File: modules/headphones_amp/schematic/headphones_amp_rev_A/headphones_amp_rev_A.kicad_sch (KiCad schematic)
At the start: 41 parts, among them J1 AudioJack3_SwitchTR, Q1 BC140, Q2 BC160, Q3 BC548, Q4 BC557, Q5 BC548, Q6 BC548, Q7 BC548, Q8 BC557

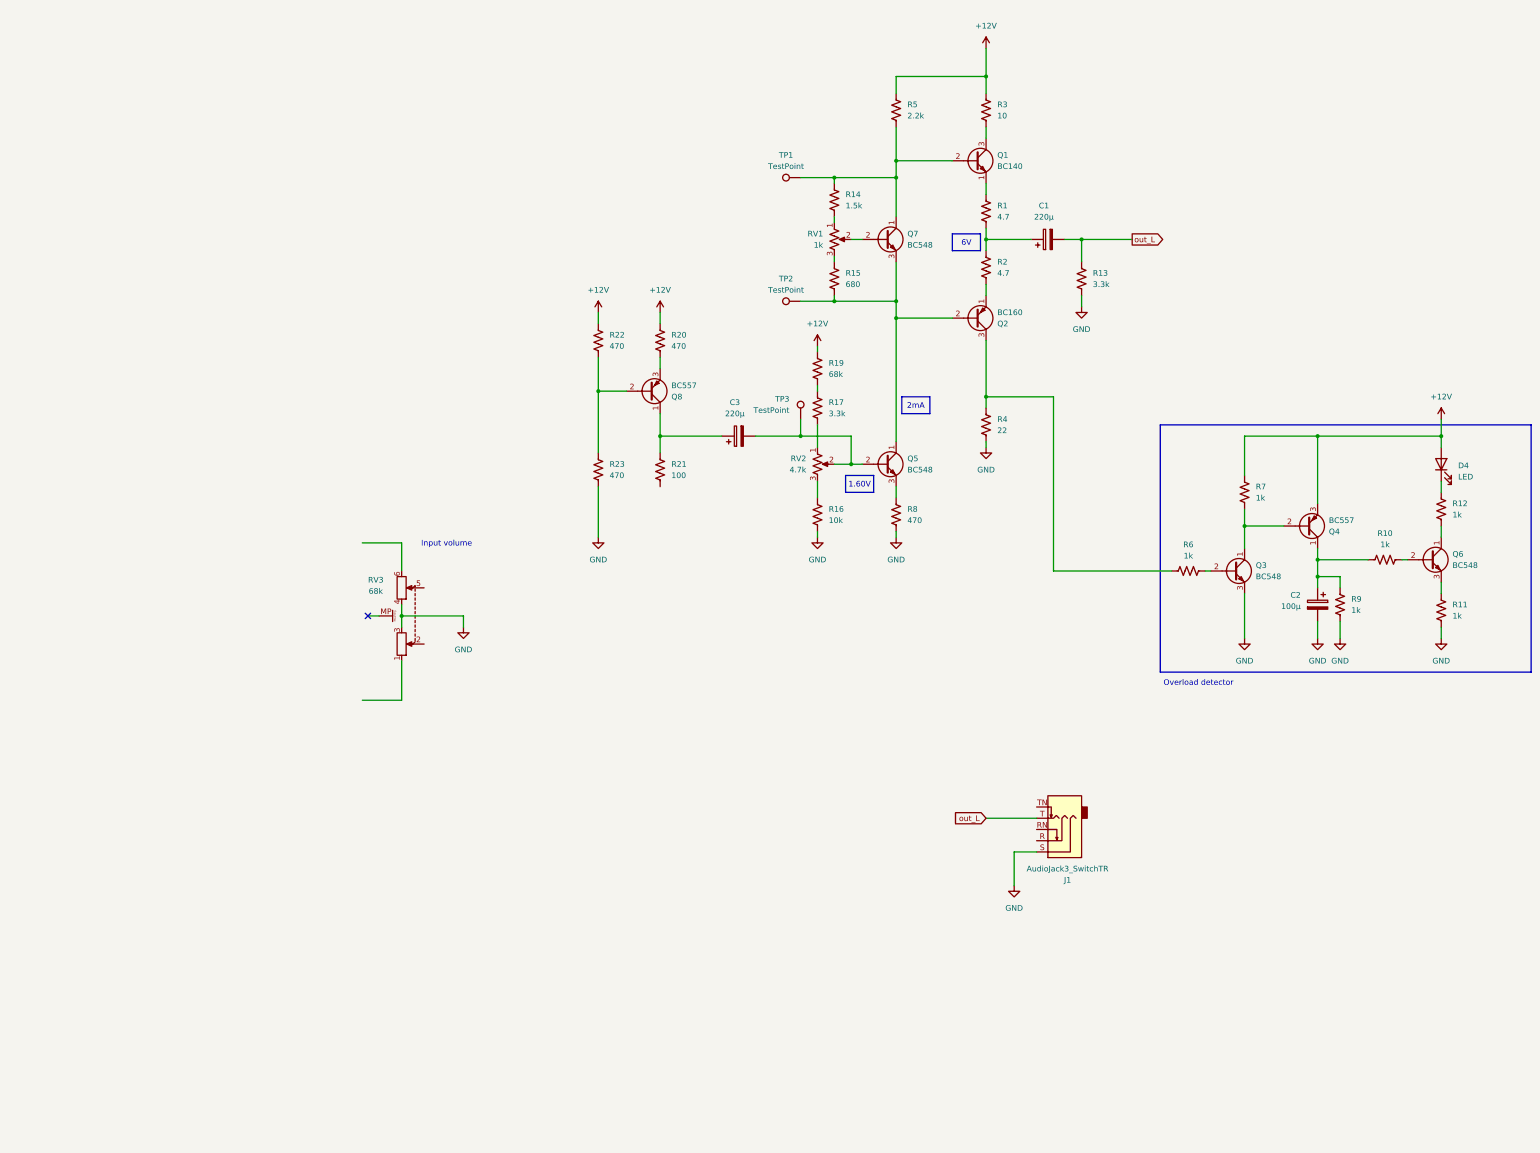
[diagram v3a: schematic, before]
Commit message: updated the Bourns PTV112 updated schematic renamed and upgraded the list of commonly used kicad parts
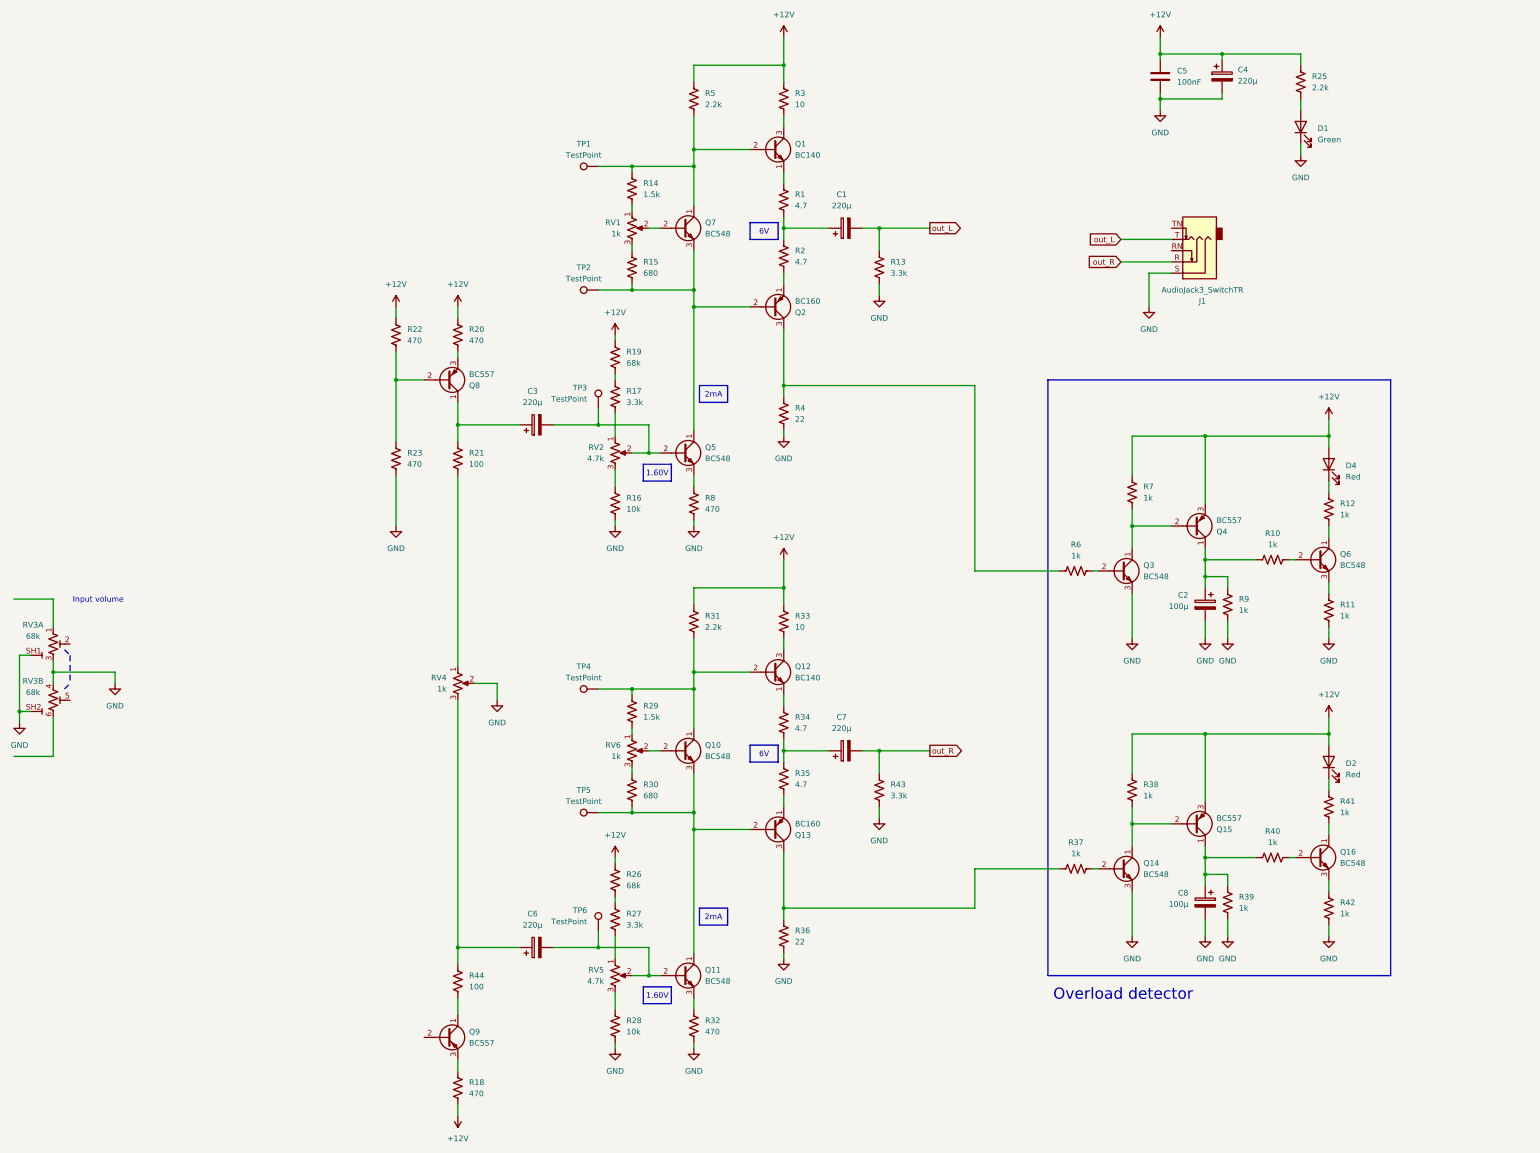
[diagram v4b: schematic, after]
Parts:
- removed RV3: 68k, Potentiometer_THT:Potentiometer_Bourns_PTV112-4_Dual_Vertical, symbol Device:R_Potentiometer_Dual_MountingPin
- added C4, C6, C7: 220µ, Capacitor_THT:CP_Radial_D10.0mm_P5.00mm, symbol Device:C_Polarized
- added C5: 100nF, Capacitor_THT:C_Rect_L7.0mm_W2.0mm_P5.00mm, symbol Device:C
- added C8: 100µ, Capacitor_THT:CP_Radial_D10.0mm_P5.00mm, symbol Device:C_Polarized
- added D1: Green, LED_THT:LED_D3.0mm, symbol Device:LED
- added D2: Red, LED_THT:LED_D3.0mm, symbol Device:LED
- added Q10, Q11, Q14, Q16: BC548, Package_TO_SOT_THT:TO-92L_Inline_Wide, symbol Transistor_BJT:BC548
- added Q12: BC140, Package_TO_SOT_THT:TO-39-3, symbol Transistor_BJT:BC140
- added Q13: BC160, Package_TO_SOT_THT:TO-39-3, symbol Transistor_BJT:BC160
- added Q15, Q9: BC557, Package_TO_SOT_THT:TO-92L_Inline_Wide, symbol Transistor_BJT:BC557
- added R18, R32: 470, Resistor_THT:R_Axial_DIN0207_L6.3mm_D2.5mm_P10.16mm_Horizontal, symbol Device:R_US
- added R25, R31: 2.2k, Resistor_THT:R_Axial_DIN0207_L6.3mm_D2.5mm_P10.16mm_Horizontal, symbol Device:R_US
- added R26: 68k, Resistor_THT:R_Axial_DIN0207_L6.3mm_D2.5mm_P10.16mm_Horizontal, symbol Device:R_US
- added R27, R43: 3.3k, Resistor_THT:R_Axial_DIN0207_L6.3mm_D2.5mm_P10.16mm_Horizontal, symbol Device:R_US
- added R28: 10k, Resistor_THT:R_Axial_DIN0207_L6.3mm_D2.5mm_P10.16mm_Horizontal, symbol Device:R_US
- added R29: 1.5k, Resistor_THT:R_Axial_DIN0207_L6.3mm_D2.5mm_P10.16mm_Horizontal, symbol Device:R_US
- added R30: 680, Resistor_THT:R_Axial_DIN0207_L6.3mm_D2.5mm_P10.16mm_Horizontal, symbol Device:R_US
- added R33: 10, Resistor_THT:R_Axial_DIN0207_L6.3mm_D2.5mm_P10.16mm_Horizontal, symbol Device:R_US
- added R34, R35: 4.7, Resistor_THT:R_Axial_DIN0207_L6.3mm_D2.5mm_P10.16mm_Horizontal, symbol Device:R_US
- added R36: 22, Resistor_THT:R_Axial_DIN0207_L6.3mm_D2.5mm_P10.16mm_Horizontal, symbol Device:R_US
- added R37, R38, R39, R40, R41, R42: 1k, Resistor_THT:R_Axial_DIN0207_L6.3mm_D2.5mm_P10.16mm_Horizontal, symbol Device:R_US
- added R44: 100, Resistor_THT:R_Axial_DIN0207_L6.3mm_D2.5mm_P10.16mm_Horizontal, symbol Device:R_US
- added RV3: 68k, ProjectLib_Transient:Potentiometer_Bourns_PTV112-4_Dual_Vertical, symbol ProjectLib_Transient:R_Potentiometer_Dual_Shield_US
- added RV4: 1k, Potentiometer_THT:Potentiometer_Alpha_RD901F-40-00D_Single_Vertical_CircularHoles, symbol Device:R_Potentiometer_US
- added RV5: 4.7k, Potentiometer_THT:Potentiometer_Bourns_3296W_Vertical, symbol Device:R_Potentiometer_US
- added RV6: 1k, Potentiometer_THT:Potentiometer_Bourns_3296W_Vertical, symbol Device:R_Potentiometer_US
- added TP4, TP5, TP6: TestPoint, TestPoint:TestPoint_Pad_D2.0mm, symbol Connector:TestPoint
- D4: value LED -> Red
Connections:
- net +12V: now also C4.1, C5.1, D2.2 (A), Q15.3 (E), R18.2, R25.1, R26.2, R31.1, R33.1, R38.1
- net GND: now also C4.2, C5.2, C8.2, D1.1 (K), Q14.3 (E), R28.2, R32.2, R36.2, R39.2, R42.2, R43.2, RV3.3, RV3.4 (1), RV3.SH1 (Shield_1), RV3.SH2 (Shield_2), RV4.2
- net out_R: now reaches J1.R
- net out_R: now also C7.2, R43.1
- net at R21.2: now also RV4.1
- new net: Q12.1 (E), R34.1
- new net: C7.1, R34.2, R35.1
- new net: R26.1, R27.1
- new net: Q16.1 (C), R41.2
- new net: Q16.2 (B), R40.2
- new net: Q16.3 (E), R42.1
- new net: R30.1, RV6.3
- new net: Q10.3 (E), Q11.1 (C), Q13.2 (B), R30.2, TP5.1
- new net: Q10.1 (C), Q12.2 (B), R29.1, R31.2, TP4.1
- new net: C6.1, R44.1, RV4.3
- new net: Q9.1 (C), R44.2
- new net: C6.2, Q11.2 (B), RV5.2, TP6.1
- new net: C8.1, Q15.1 (C), R39.1, R40.1
- new net: Q14.1 (C), Q15.2 (B), R38.2
- new net: Q14.2 (B), R37.2
- new net: R27.2, RV5.1
- new net: R28.1, RV5.3
- new net: D1.2 (A), R25.2
- new net: Q11.3 (E), R32.1
- new net: Q10.2 (B), RV6.2
- new net: R29.2, RV6.1
- new net: D2.1 (K), R41.1
- new net: Q9.3 (E), R18.1
- new net: Q12.3 (C), R33.2
- new net: Q13.1 (E), R35.2
- new net: Q13.3 (C), R36.1, R37.1
- no-connect marks 1 -> 0
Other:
- moved on the sheet: C1, C2, C3, D4, J1, Q1, Q2, Q3, Q4, Q5, Q6, Q7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

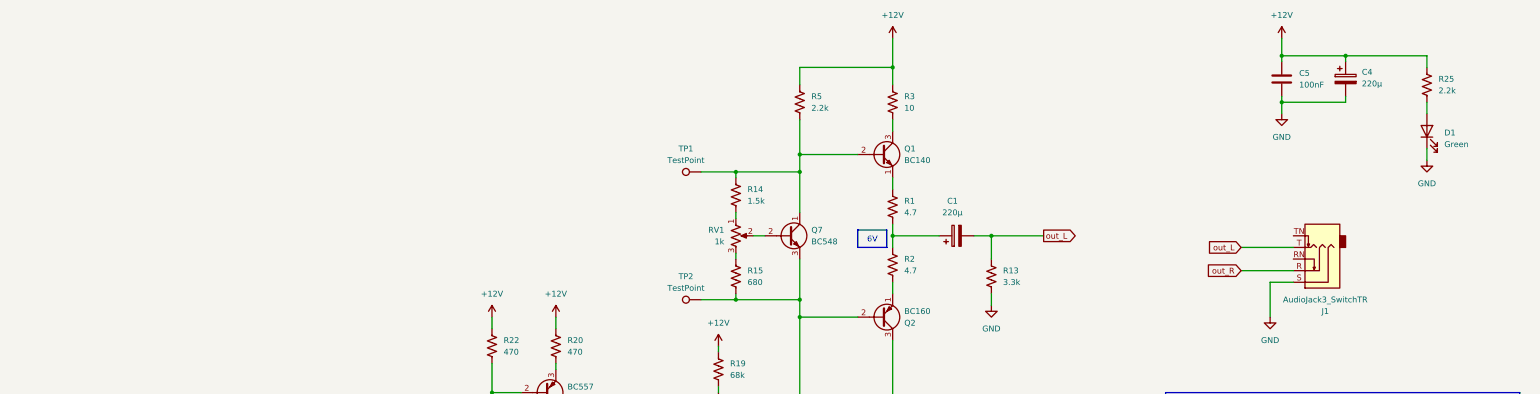
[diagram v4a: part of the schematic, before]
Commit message: added footprint for the ANT switch
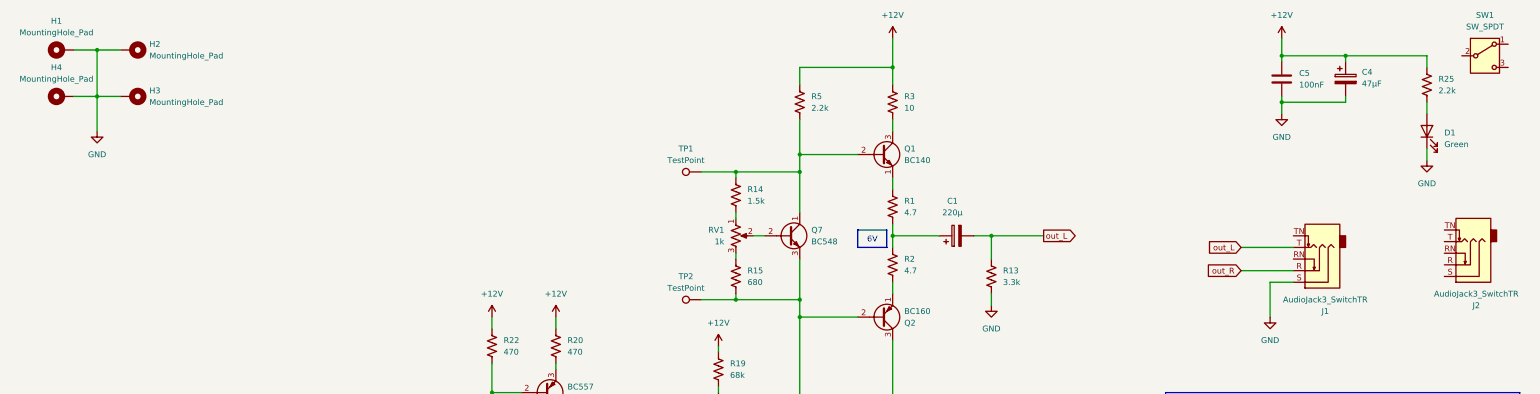
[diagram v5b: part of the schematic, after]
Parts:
- added H1, H2, H3, H4: MountingHole_Pad, MountingHole:MountingHole_3.2mm_M3_Pad_Via, symbol Mechanical:MountingHole_Pad
- added J2: AudioJack3_SwitchTR, Connector_Audio:Jack_3.5mm_CUI_SJ1-3515N_Horizontal, symbol Connector_Audio:AudioJack3_SwitchTR
- added SW1: SW_SPDT, Button_Switch_SMD:SW_SPST_Omron_B3FS-100xP, symbol Switch:SW_SPDT
- C4: value 220µ -> 47µF
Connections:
- net GND: now also H1.1, H2.1, H3.1, H4.1

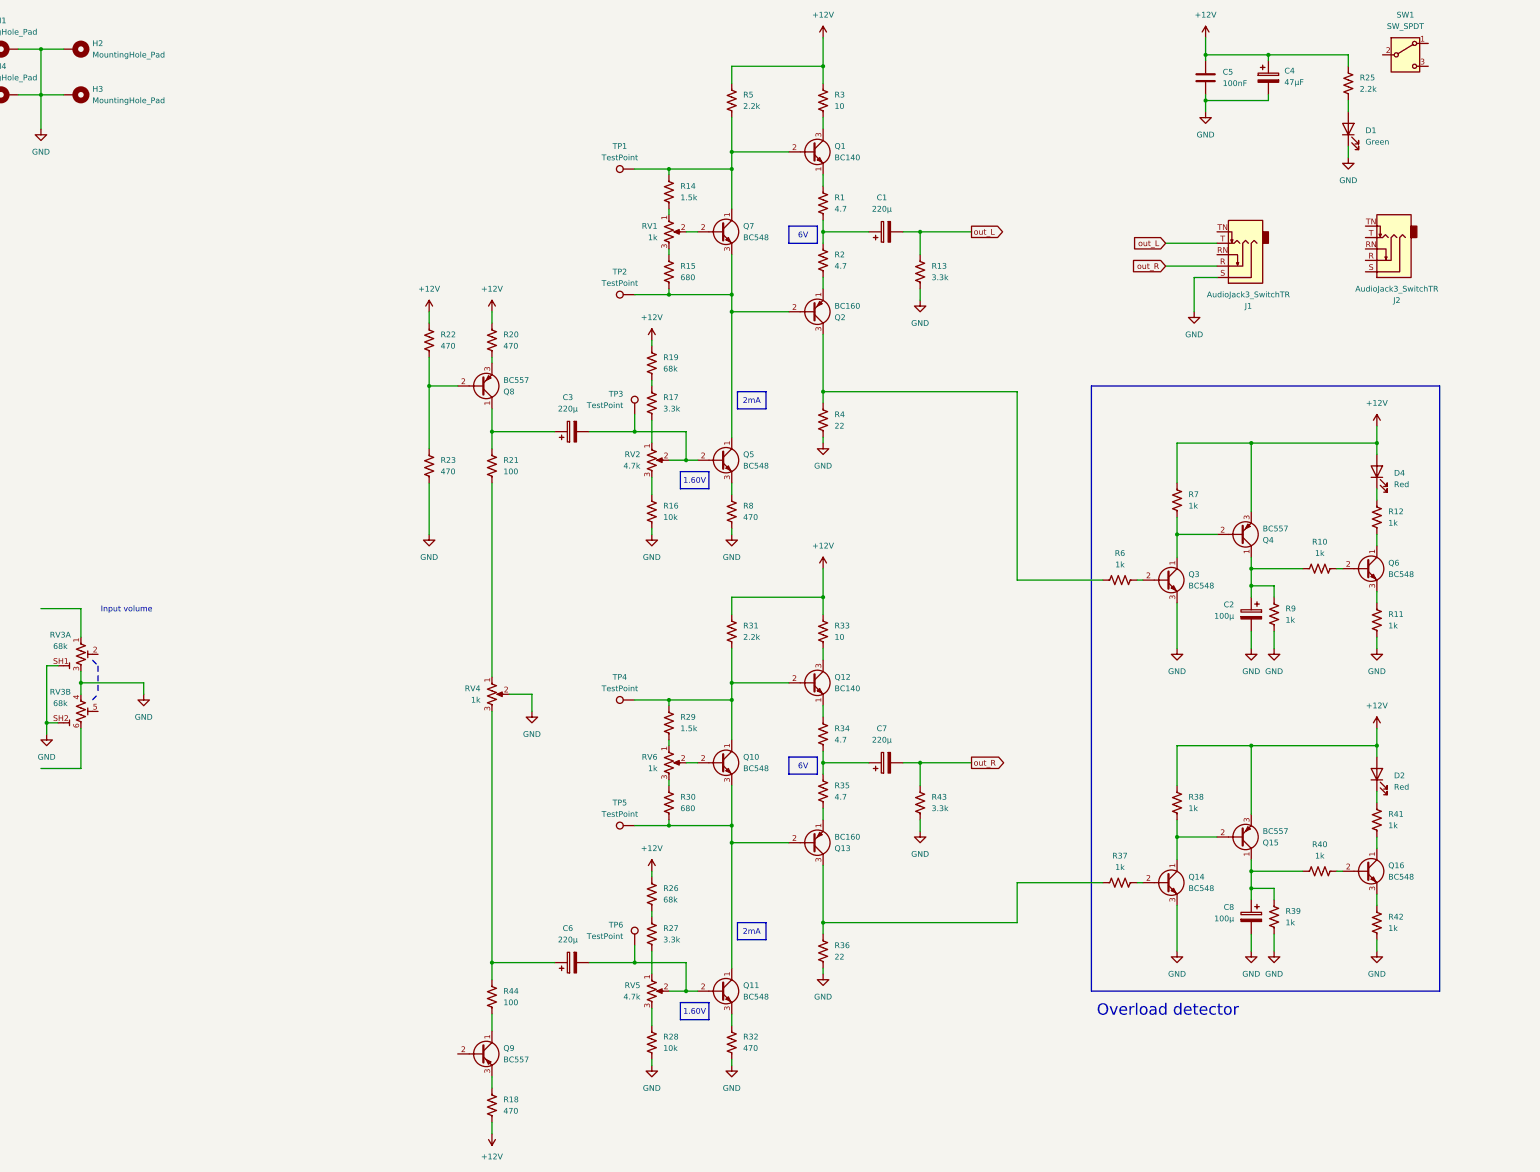
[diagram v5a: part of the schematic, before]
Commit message: updated ignore list updated library with a new switch (ANT)
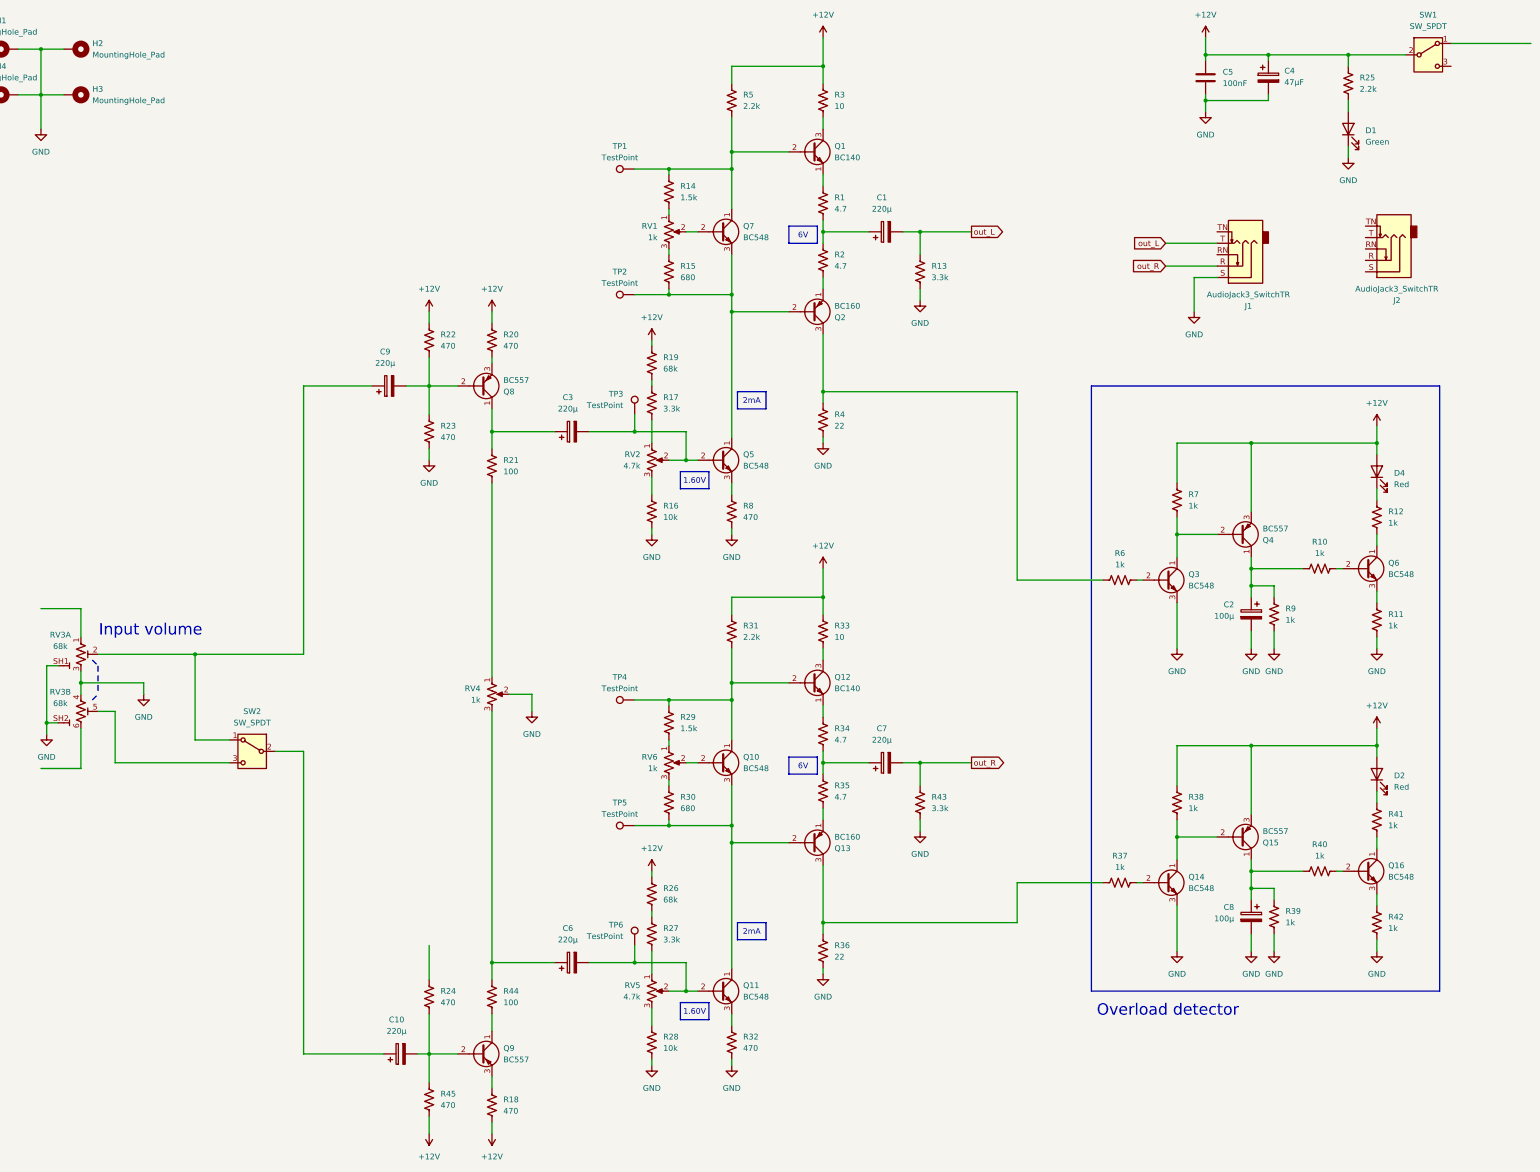
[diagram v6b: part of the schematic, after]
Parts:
- removed SW1: SW_SPDT, Button_Switch_SMD:SW_SPST_Omron_B3FS-100xP, symbol Switch:SW_SPDT
- added C10, C9: 220µ, Capacitor_THT:CP_Radial_D10.0mm_P5.00mm, symbol Device:C_Polarized
- added R24, R45: 470, Resistor_THT:R_Axial_DIN0207_L6.3mm_D2.5mm_P10.16mm_Horizontal, symbol Device:R_US
- added SW1, SW2: SW_SPDT, ProjectLib_Transient:SW_CIT_ANT13_SPDT_Straight, symbol ProjectLib_Transient:SW_SPDT
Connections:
- net +12V: now also R45.2, SW1.2
- net at RV3.5 (2): now also SW2.3
- net at Q8.2 (B), R22.2, R23.1: now also C9.2
- net at Q9.2 (B): now also C10.2, R24.2, R45.1
- net at RV3.2: now also C9.1, SW2.1
- new net: C10.1, SW2.2
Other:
- moved on the sheet: R23
